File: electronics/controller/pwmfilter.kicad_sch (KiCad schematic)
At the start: 21 parts, among them U10 MC33204

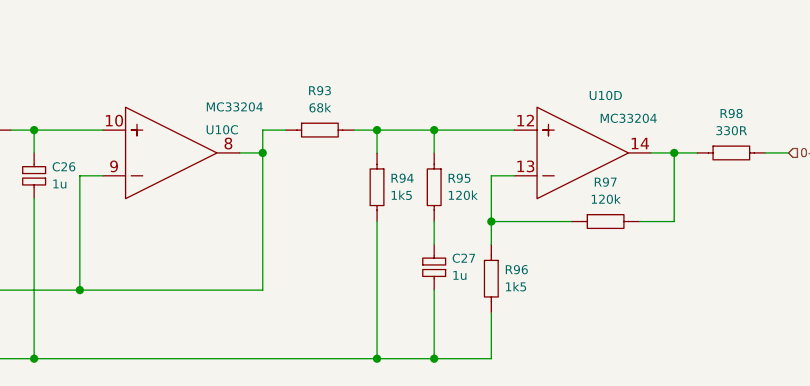
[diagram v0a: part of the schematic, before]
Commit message: Adjust the output gain of the 0-10V outputs
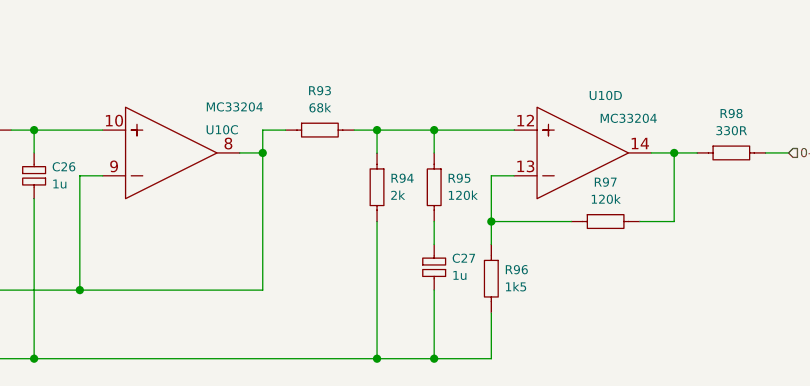
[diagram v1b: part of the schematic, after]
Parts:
- R94: value 1k5 -> 2k
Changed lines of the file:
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@@
       (effects (font (size 0.9906 0.9906)) (justify left))
     )
-    (property "Value" "1k5" (id 1) (at 232.6132 91.1098 90)
+    (property "Value" "2k" (id 1) (at 232.6132 91.1098 90)
       (effects (font (size 0.9906 0.9906)) (justify left))
     )
